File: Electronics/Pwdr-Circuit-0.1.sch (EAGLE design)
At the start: 23 parts, among them U1 LM317T, U2 ARDUINO-MEGASHIELD, U5 ULN2003, U6 ULN2003

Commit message: Removed bug from electronic diagrams
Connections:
- net AGND: now also C2.+, R1.1, U1.OUT; no longer C2.-, U5.CD+, U6.CD+
- net N$2: now also C2.-, U5.CD+, U6.CD+; no longer C2.+, R1.1, U1.OUT

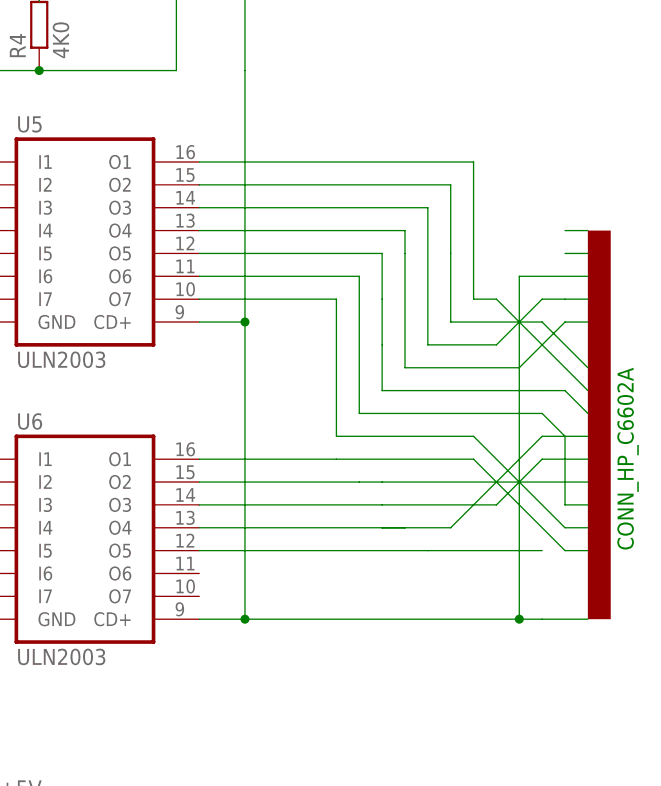
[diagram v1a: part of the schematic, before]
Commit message: Corrected wiring to HP Conn.
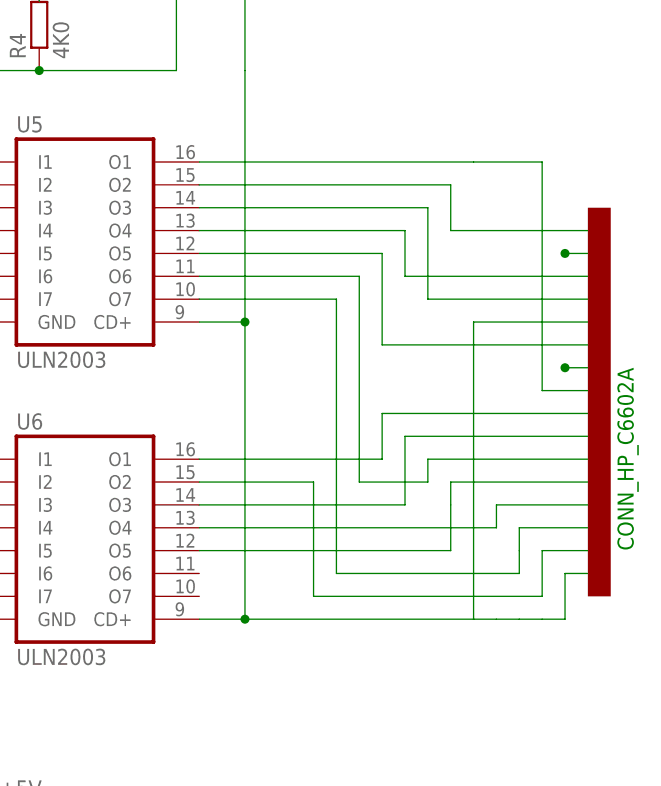
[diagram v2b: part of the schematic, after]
